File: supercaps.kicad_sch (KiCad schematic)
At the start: 24 parts, among them J7 XT30_F, J8 XT30_F

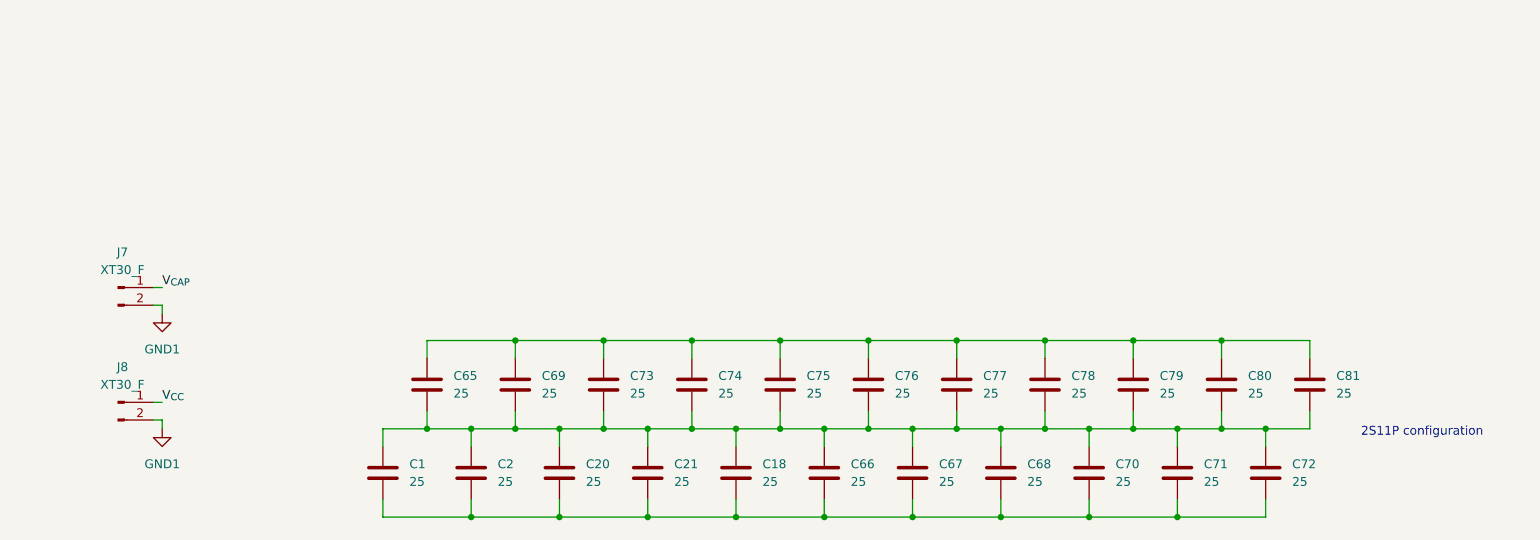
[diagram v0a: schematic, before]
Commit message: Adding simulation for charging & balancing
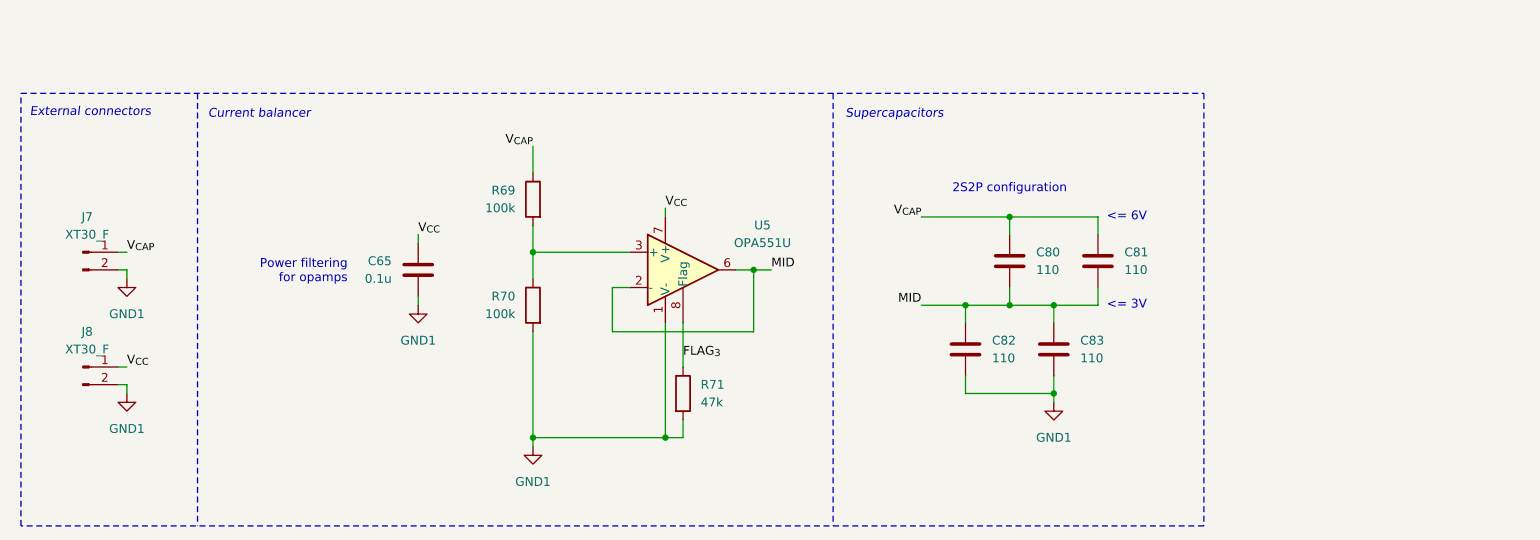
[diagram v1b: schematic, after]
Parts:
- removed C1, C18, C2, C20, C21, C66, C67, C68, C69, C70, C71, C72, C73, C74, C75, C76, C77, C78, C79: 25, symbol Device:C
- added C82, C83: 110, Capacitor_THT:C_Radial_D18.0mm_H35.5mm_P7.50mm, symbol Device:C
- added R69, R70: 100k, Resistor_SMD:R_0603_1608Metric_Pad0.98x0.95mm_HandSolder, symbol Device:R
- added R71: 47k, Resistor_SMD:R_0603_1608Metric_Pad0.98x0.95mm_HandSolder, symbol Device:R
- added U5: OPA551U, Package_SO:SOIC-8_3.9x4.9mm_P1.27mm, symbol Amplifier_Operational:OPA551U
- C65: value 25 -> 0.1u; footprint (none) -> Capacitor_SMD:C_0603_1608Metric_Pad1.08x0.95mm_HandSolder; Mouser Part Number 581-SCCU25B256SRB -> (none)
- C80, C81: value 25 -> 110; footprint (none) -> Capacitor_THT:C_Radial_D18.0mm_H35.5mm_P7.50mm; Mouser Part Number 581-SCCU25B256SRB -> 598-DSF117Q3R0
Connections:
- net GND1: now also C65.2, C82.2, C83.2, R70.2, R71.2, U5.1 (V-), U5.4 (V-), U5.5 (V-)
- net V_{CAP}: now also C80.1, C81.1, R69.1
- net V_{CC}: now also C65.1, U5.7 (V+)
- net MID: now reaches C80.2, C81.2
- net MID: now also C82.1, C83.1, U5.2 (-), U5.6; no longer C65.2
- new net: R69.2, R70.1, U5.3 (+)
- new net FLAG_{3}: R71.1, U5.8 (Flag)
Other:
- note added: "2S2P configuration"
- note added: "<= 3V"
- note added: "<= 6V"
- note added: "Current balancer"
- note added: "External connectors"
- note added: "Power filtering for opamps"
- note added: "Supercapacitors"
- note removed: "2S11P configuration"
- title: (none) -> Supercapacitor + Balancing
- moved on the sheet: C80, J7, J8

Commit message: Finalize balancing circuit
Looks pretty stable to me
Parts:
- removed U5: OPA551U, Package_SO:SOIC-8_3.9x4.9mm_P1.27mm, symbol Amplifier_Operational:OPA551U
- added C18: 100p, Capacitor_SMD:C_0603_1608Metric_Pad1.08x0.95mm_HandSolder, symbol Device:C
- added Q2: Q_NPN_BCE, symbol Transistor_BJT:Q_NPN_BCE
- added Q5: Q_PNP_BCE, symbol Transistor_BJT:Q_PNP_BCE
- added R72: 100, Resistor_SMD:R_0603_1608Metric_Pad0.98x0.95mm_HandSolder, symbol Device:R
- added R73, R74: 0.2, Resistor_SMD:R_0603_1608Metric_Pad0.98x0.95mm_HandSolder, symbol Device:R
- added U5: TLV9301xDBV, Package_TO_SOT_SMD:SOT-23-5_HandSoldering, symbol Amplifier_Operational:TLV9301xDBV
- R69, R70: value 100k -> 1Meg
- R71: value 47k -> 1k
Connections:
- net FLAG_{3} is gone; now on net MID: R71.1
- net GND1: now also Q5.2 (C), U5.2 (V-); no longer R71.2
- net MID: now also R72.2, R73.2, R74.1
- net V_{CC}: now also Q2.2 (C), U5.5 (V+)
- net REF: now reaches R69.2, R70.1
- net REF: now also U5.3 (+)
- new net LOWER_R: Q5.3 (E), R74.2
- new net OP_OUT: C18.2, Q2.1 (B), Q5.1 (B), R72.1, U5.1
- new net UPPER_R: Q2.3 (E), R73.1
- new net V-: C18.1, R71.2, U5.4 (-)
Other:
- note added: "Typ. +6V from GND1"
- moved on the sheet: C65, C80, C81, C82, C83, J7, J8, R69, R70

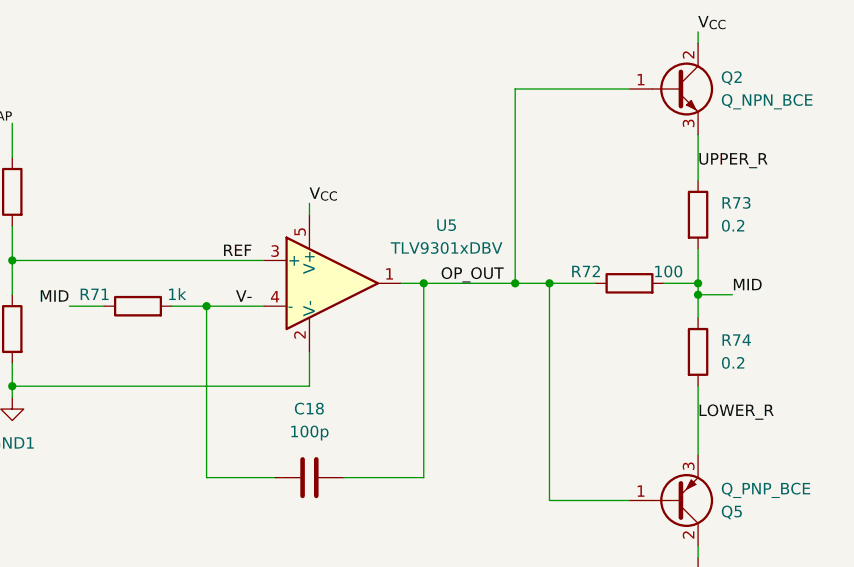
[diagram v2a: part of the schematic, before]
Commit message: Adjust values for better feedback
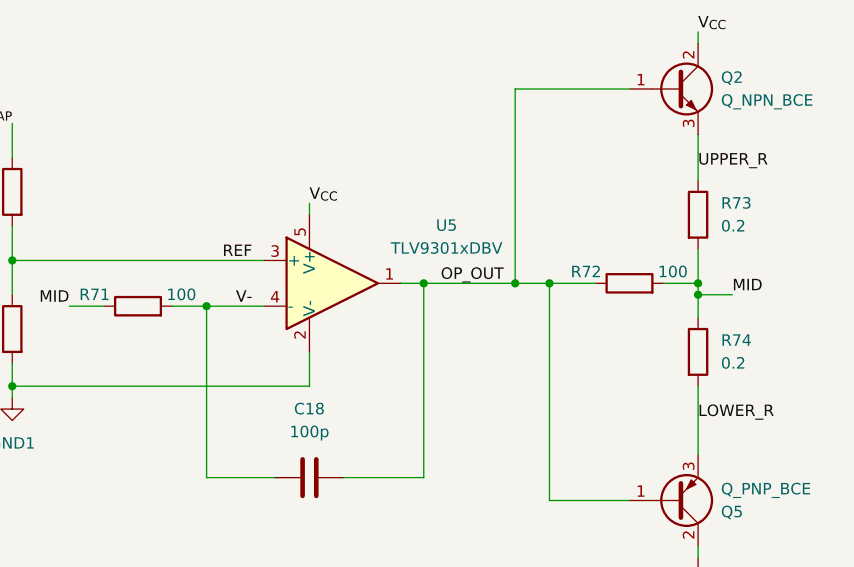
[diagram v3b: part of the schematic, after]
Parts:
- R71: value 1k -> 100
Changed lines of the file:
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@@
 			)
 		)
-		(property "Value" "1k"
-			(at 65.278 59.69 90)
+		(property "Value" "100"
+			(at 65.786 59.69 90)
 			(effects
 				(font
@@
 		)
 		(property "Value" "100"
-			(at 119.888 57.15 90)
+			(at 120.396 57.15 90)
 			(effects
 				(font

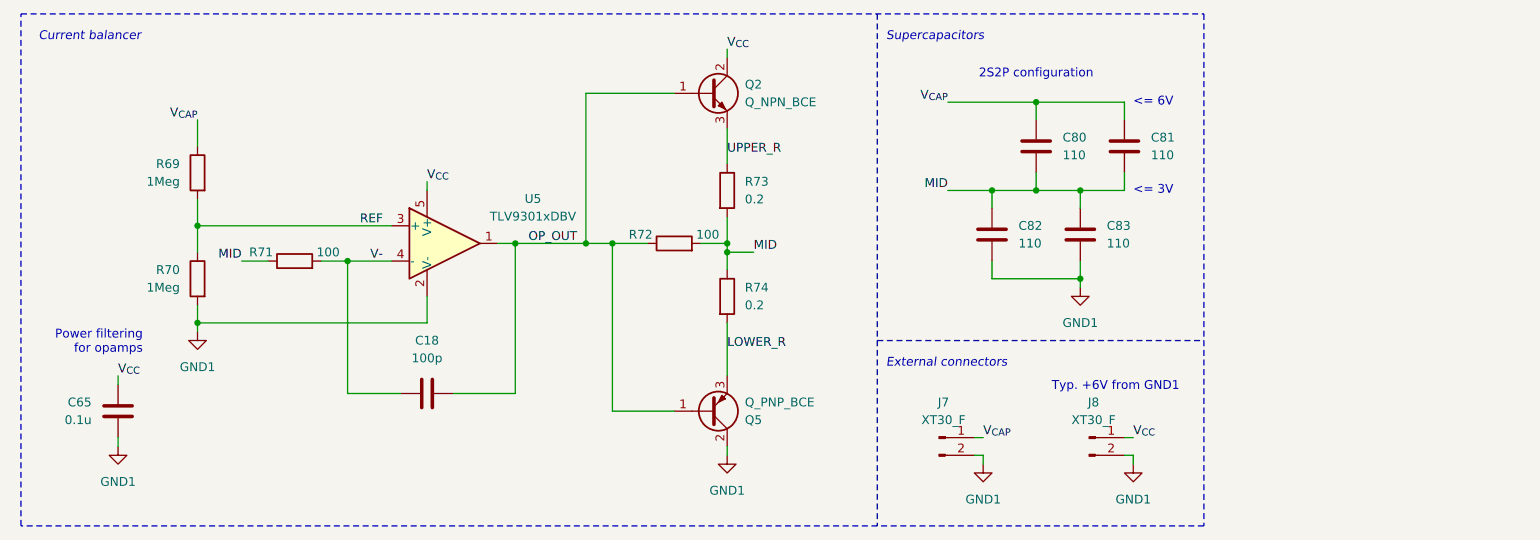
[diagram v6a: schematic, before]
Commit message: Reannotate schematic
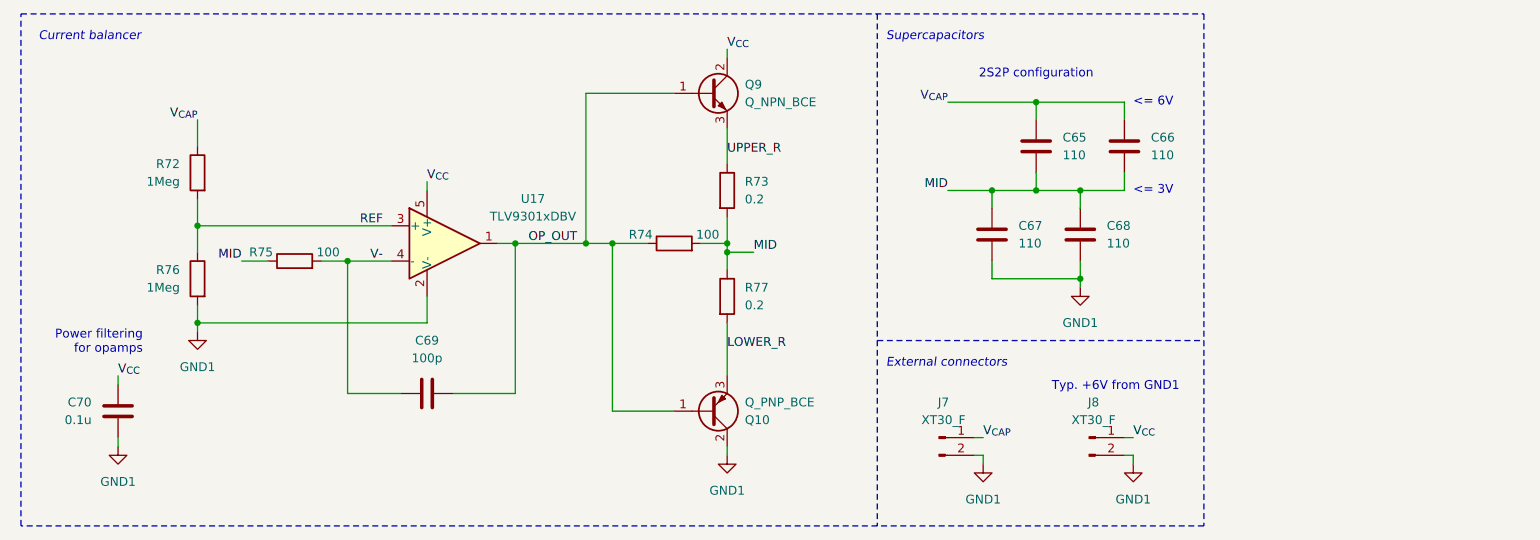
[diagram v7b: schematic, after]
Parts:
- renumbered C80 to C65, C81 to C66, C82 to C67, C83 to C68, C18 to C69, C65 to C70, Q5 to Q10, Q2 to Q9, R69 to R72, R72 to R74, R71 to R75, R70 to R76, R74 to R77, U5 to U17
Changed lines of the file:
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@@
 		(on_board yes)
 		(dnp no)
-		(property "Reference" "R74"
+		(property "Reference" "R77"
 			(at 125.73 64.7699 0)
 			(effects
@@
 			(project "SupercapManager"
 				(path "/6197145b-e7d4-44cc-9d90-537b6501bf60/e69614f9-5cd8-4aa3-ae42-53f80cb78886"
-					(reference "R74")
+					(reference "R77")
 					(unit 1)
 				)
@@
 		(on_board yes)
 		(dnp no)
-		(property "Reference" "U5"
+		(property "Reference" "U17"
 			(at 95.25 51.9998 0)
 			(effects
@@
 			(project ""
 				(path "/6197145b-e7d4-44cc-9d90-537b6501bf60/e69614f9-5cd8-4aa3-ae42-53f80cb78886"
-					(reference "U5")
+					(reference "U17")
 					(unit 1)
 				)
@@
 		(dnp no)
 		(fields_autoplaced yes)
-		(property "Reference" "C18"
+		(property "Reference" "C69"
 			(at 80.01 72.39 90)
 			(effects
@@
 			(project ""
 				(path "/6197145b-e7d4-44cc-9d90-537b6501bf60/e69614f9-5cd8-4aa3-ae42-53f80cb78886"
-					(reference "C18")
+					(reference "C69")
 					(unit 1)
 				)
@@
 		(dnp no)
 		(fields_autoplaced yes)
-		(property "Reference" "C82"
+		(property "Reference" "C67"
 			(at 165.1 55.8799 0)
 			(effects
@@
 			(project "SupercapManager"
 				(path "/6197145b-e7d4-44cc-9d90-537b6501bf60/e69614f9-5cd8-4aa3-ae42-53f80cb78886"
-					(reference "C82")
+					(reference "C67")
 					(unit 1)
 				)
@@
 		(dnp no)
 		(fields_autoplaced yes)
-		(property "Reference" "#PWR056"
+		(property "Reference" "#PWR099"
 			(at 46.99 77.47 0)
 			(effects
@@
 			(project "SupercapManager"
 				(path "/6197145b-e7d4-44cc-9d90-537b6501bf60/e69614f9-5cd8-4aa3-ae42-53f80cb78886"
-					(reference "#PWR056")
+					(reference "#PWR099")
 					(unit 1)
 				)
@@
 		(dnp no)
 		(fields_autoplaced yes)
-		(property "Reference" "C65"
+		(property "Reference" "C70"
 			(at 31.75 81.2799 0)
 			(effects
@@
 			(project "SupercapManager"
 				(path "/6197145b-e7d4-44cc-9d90-537b6501bf60/e69614f9-5cd8-4aa3-ae42-53f80cb78886"
-					(reference "C65")
+					(reference "C70")
 					(unit 1)
 				)
@@
 		(dnp no)
 		(fields_autoplaced yes)
-		(property "Reference" "#PWR053"
+		(property "Reference" "#PWR0102"
 			(at 160.02 96.52 0)
 			(effects
@@
 			(project ""
 				(path "/6197145b-e7d4-44cc-9d90-537b6501bf60/e69614f9-5cd8-4aa3-ae42-53f80cb78886"
-					(reference "#PWR053")
+					(reference "#PWR0102")
 					(unit 1)
 				)
@@
 		(dnp no)
 		(fields_autoplaced yes)
-		(property "Reference" "#PWR055"
+		(property "Reference" "#PWR098"
 			(at 173.99 71.12 0)
 			(effects
@@
 			(project "SupercapManager"
 				(path "/6197145b-e7d4-44cc-9d90-537b6501bf60/e69614f9-5cd8-4aa3-ae42-53f80cb78886"
-					(reference "#PWR055")
+					(reference "#PWR098")
 					(unit 1)
 				)
@@
 		(on_board yes)
 		(dnp no)
-		(property "Reference" "R69"
+		(property "Reference" "R72"
 			(at 44.45 46.9899 0)
 			(effects
@@
 			(project ""
 				(path "/6197145b-e7d4-44cc-9d90-537b6501bf60/e69614f9-5cd8-4aa3-ae42-53f80cb78886"
-					(reference "R69")
+					(reference "R72")
 					(unit 1)
 				)
@@
 		(dnp no)
 		(fields_autoplaced yes)
-		(property "Reference" "C80"
+		(property "Reference" "C65"
 			(at 171.45 43.1799 0)
 			(effects
@@
 			(project "SupercapManager"
 				(path "/6197145b-e7d4-44cc-9d90-537b6501bf60/e69614f9-5cd8-4aa3-ae42-53f80cb78886"
-					(reference "C80")
+					(reference "C65")
 					(unit 1)
 				)
@@
 		(dnp no)
 		(fields_autoplaced yes)
-		(property "Reference" "#PWR058"
+		(property "Reference" "#PWR0101"
 			(at 123.19 95.25 0)
 			(effects
@@
 			(project "SupercapManager"
 				(path "/6197145b-e7d4-44cc-9d90-537b6501bf60/e69614f9-5cd8-4aa3-ae42-53f80cb78886"
-					(reference "#PWR058")
+					(reference "#PWR0101")
 					(unit 1)
 				)
@@
 		(dnp no)
 		(fields_autoplaced yes)
-		(property "Reference" "Q2"
+		(property "Reference" "Q9"
 			(at 125.73 35.5599 0)
 			(effects
@@
 			(project ""
 				(path "/6197145b-e7d4-44cc-9d90-537b6501bf60/e69614f9-5cd8-4aa3-ae42-53f80cb78886"
-					(reference "Q2")
+					(reference "Q9")
 					(unit 1)
 				)
@@
 		(dnp no)
 		(fields_autoplaced yes)
-		(property "Reference" "C81"
+		(property "Reference" "C66"
 			(at 184.15 43.1799 0)
 			(effects
@@
 			(project "SupercapManager"
 				(path "/6197145b-e7d4-44cc-9d90-537b6501bf60/e69614f9-5cd8-4aa3-ae42-53f80cb78886"
-					(reference "C81")
+					(reference "C66")
 					(unit 1)
 				)
@@
 		(on_board yes)
 		(dnp no)
-		(property "Reference" "R70"
+		(property "Reference" "R76"
 			(at 44.45 62.2299 0)
 			(effects
@@
 			(project "SupercapManager"
 				(path "/6197145b-e7d4-44cc-9d90-537b6501bf60/e69614f9-5cd8-4aa3-ae42-53f80cb78886"
-					(reference "R70")
+					(reference "R76")
 					(unit 1)
 				)
@@
 		(on_board yes)
 		(dnp no)
-		(property "Reference" "R71"
+		(property "Reference" "R75"
 			(at 56.134 59.69 90)
 			(effects
@@
 			(project ""
 				(path "/6197145b-e7d4-44cc-9d90-537b6501bf60/e69614f9-5cd8-4aa3-ae42-53f80cb78886"
-					(reference "R71")
+					(reference "R75")
 					(unit 1)
 				)
@@
 		(dnp no)
 		(fields_autoplaced yes)
-		(property "Reference" "#PWR057"
+		(property "Reference" "#PWR0100"
 			(at 35.56 93.98 0)
 			(effects
@@
 			(project "SupercapManager"
 				(path "/6197145b-e7d4-44cc-9d90-537b6501bf60/e69614f9-5cd8-4aa3-ae42-53f80cb78886"
-					(reference "#PWR057")
+					(reference "#PWR0100")
 					(unit 1)
 				)
@@
 		(dnp no)
 		(fields_autoplaced yes)
-		(property "Reference" "#PWR054"
+		(property "Reference" "#PWR0103"
 			(at 181.61 96.52 0)
 			(effects
@@
 			(project "SupercapManager"
 				(path "/6197145b-e7d4-44cc-9d90-537b6501bf60/e69614f9-5cd8-4aa3-ae42-53f80cb78886"
-					(reference "#PWR054")
+					(reference "#PWR0103")
 					(unit 1)
 				)
@@
 		(on_board yes)
 		(dnp no)
-		(property "Reference" "R72"
+		(property "Reference" "R74"
 			(at 110.744 57.15 90)
 			(effects
@@
 			(project "SupercapManager"
 				(path "/6197145b-e7d4-44cc-9d90-537b6501bf60/e69614f9-5cd8-4aa3-ae42-53f80cb78886"
-					(reference "R72")
+					(reference "R74")
 					(unit 1)
 				)
@@
 		(on_board yes)
 		(dnp no)
-		(property "Reference" "Q5"
+		(property "Reference" "Q10"
 			(at 125.73 83.8201 0)
 			(effects
@@
 			(project ""
 				(path "/6197145b-e7d4-44cc-9d90-537b6501bf60/e69614f9-5cd8-4aa3-ae42-53f80cb78886"
-					(reference "Q5")
+					(reference "Q10")
 					(unit 1)
 				)
@@
 		(dnp no)
 		(fields_autoplaced yes)
-		(property "Reference" "C83"
+		(property "Reference" "C68"
 			(at 177.8 55.8799 0)
 			(effects
@@
 			(project "SupercapManager"
 				(path "/6197145b-e7d4-44cc-9d90-537b6501bf60/e69614f9-5cd8-4aa3-ae42-53f80cb78886"
-					(reference "C83")
-					(unit 1)
-				)
+					(reference "C68")
+					(unit 1)
+				)

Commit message: Finalized design !!!
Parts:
- R73, R77: value 0.2 -> 0.1
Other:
- note added: "Typ. +5V from GND1"
- note removed: "Typ. +6V from GND1"
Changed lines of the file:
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@@
 		)
 	)
-	(text "Typ. +6V from GND1"
+	(text "Typ. +5V from GND1"
 		(exclude_from_sim no)
 		(at 179.07 79.756 0)
@@
 			)
 		)
-		(property "Value" "0.2"
+		(property "Value" "0.1"
 			(at 125.73 67.3099 0)
 			(effects
@@
 			)
 		)
-		(property "Value" "0.2"
+		(property "Value" "0.1"
 			(at 125.73 52.0699 0)
 			(effects
